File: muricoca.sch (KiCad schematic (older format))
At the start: 49 parts, among them J1 USB_B_Mini, SW1 Esc, SW10 9, SW11 0, SW12 -, SW13 =, SW14 Bksp, SW15 MXSwitch, SW16 MXSwitch, SW2 1, SW3 2, SW4 3, SW5 4, SW6 5, SW7 6, SW8 7, SW9 8, U1 ATmega32U4-AU, Y1 16Mhz

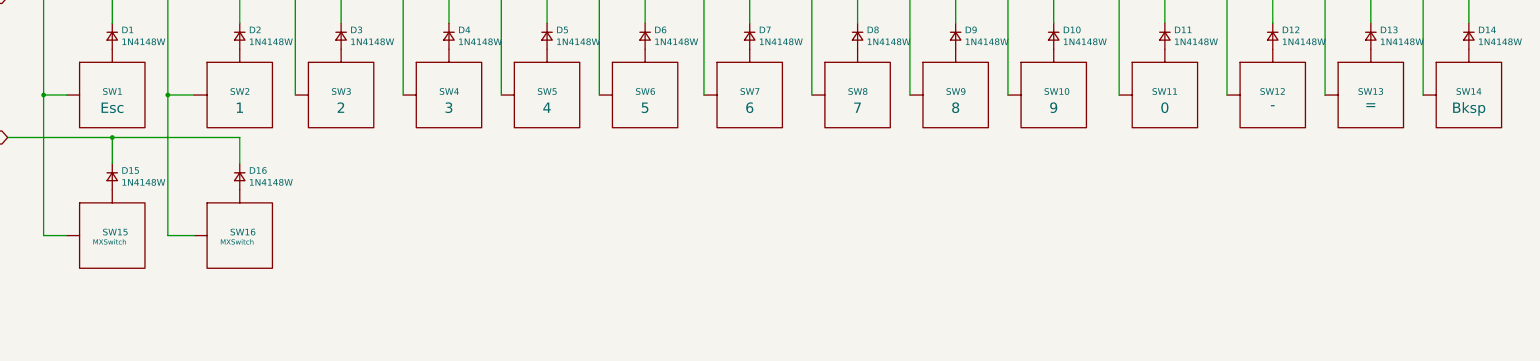
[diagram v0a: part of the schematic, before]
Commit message: feat: add matrix second row
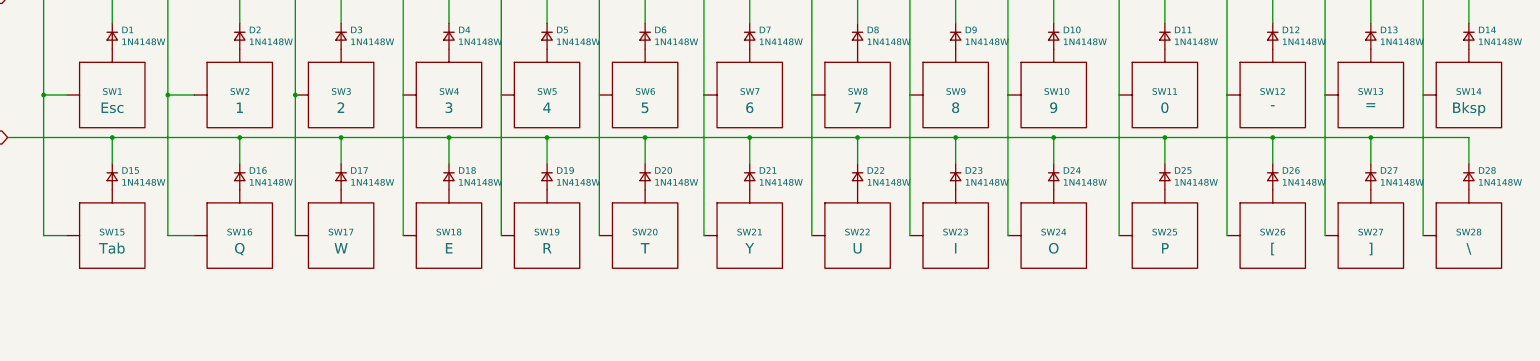
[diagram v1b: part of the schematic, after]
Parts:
- added D17, D18, D19, D20, D21, D22, D23, D24, D25, D26, D27, D28: 1N4148W, Diode_SMD:D_SOD-123, symbol Device:D_Small
- added SW17: W, acheron_MX:MX100, symbol acheronSymbols:MXSwitch
- added SW18: E, acheron_MX:MX100, symbol acheronSymbols:MXSwitch
- added SW19: R, acheron_MX:MX100, symbol acheronSymbols:MXSwitch
- added SW20: T, acheron_MX:MX100, symbol acheronSymbols:MXSwitch
- added SW21: Y, acheron_MX:MX100, symbol acheronSymbols:MXSwitch
- added SW22: U, acheron_MX:MX100, symbol acheronSymbols:MXSwitch
- added SW23: I, acheron_MX:MX100, symbol acheronSymbols:MXSwitch
- added SW24: O, acheron_MX:MX100, symbol acheronSymbols:MXSwitch
- added SW25: P, acheron_MX:MX100, symbol acheronSymbols:MXSwitch
- added SW26: [, acheron_MX:MX100, symbol acheronSymbols:MXSwitch
- added SW27: ], acheron_MX:MX100, symbol acheronSymbols:MXSwitch
- added SW28: \\, acheron_MX:MX100, symbol acheronSymbols:MXSwitch
- SW15: value MXSwitch -> Tab
- SW16: value MXSwitch -> Q
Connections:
- net COL10: now also SW24.1 (Col)
- net COL11: now also SW25.1 (Col)
- net COL12: now also SW26.1 (Col)
- net COL13: now also SW27.1 (Col)
- net COL14: now also SW28.1 (Col)
- net COL3: now also SW17.1 (Col)
- net COL4: now also SW18.1 (Col)
- net COL5: now also SW19.1 (Col)
- net COL6: now also SW20.1 (Col)
- net COL7: now also SW21.1 (Col)
- net COL8: now also SW22.1 (Col)
- net COL9: now also SW23.1 (Col)
- net ROW2: now also D17.1 (K), D18.1 (K), D19.1 (K), D20.1 (K), D21.1 (K), D22.1 (K), D23.1 (K), D24.1 (K), D25.1 (K), D26.1 (K), D27.1 (K), D28.1 (K)
- new net: D17.2 (A), SW17.2 (Row)
- new net: D18.2 (A), SW18.2 (Row)
- new net: D19.2 (A), SW19.2 (Row)
- new net: D20.2 (A), SW20.2 (Row)
- new net: D21.2 (A), SW21.2 (Row)
- new net: D22.2 (A), SW22.2 (Row)
- new net: D23.2 (A), SW23.2 (Row)
- new net: D24.2 (A), SW24.2 (Row)
- new net: D25.2 (A), SW25.2 (Row)
- new net: D26.2 (A), SW26.2 (Row)
- new net: D27.2 (A), SW27.2 (Row)
- new net: D28.2 (A), SW28.2 (Row)

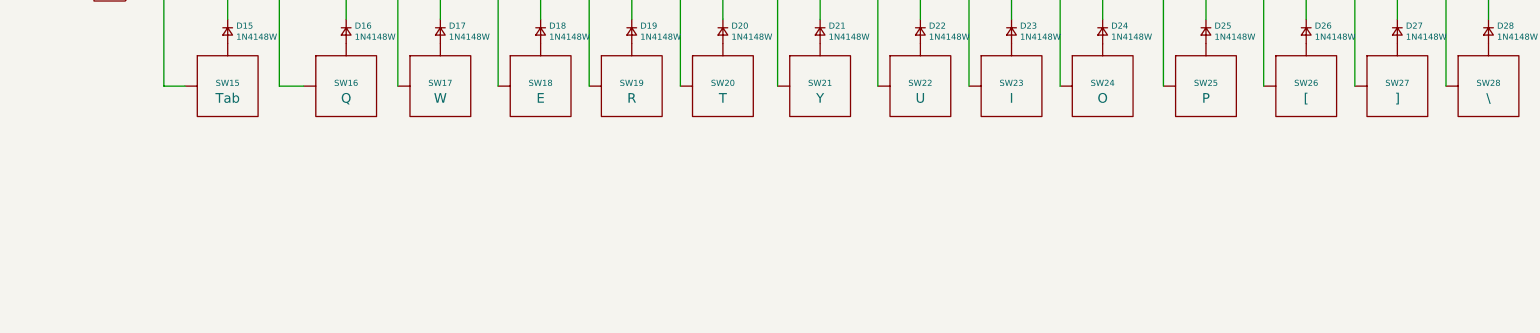
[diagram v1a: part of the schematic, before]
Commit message: feat: add matrix third row
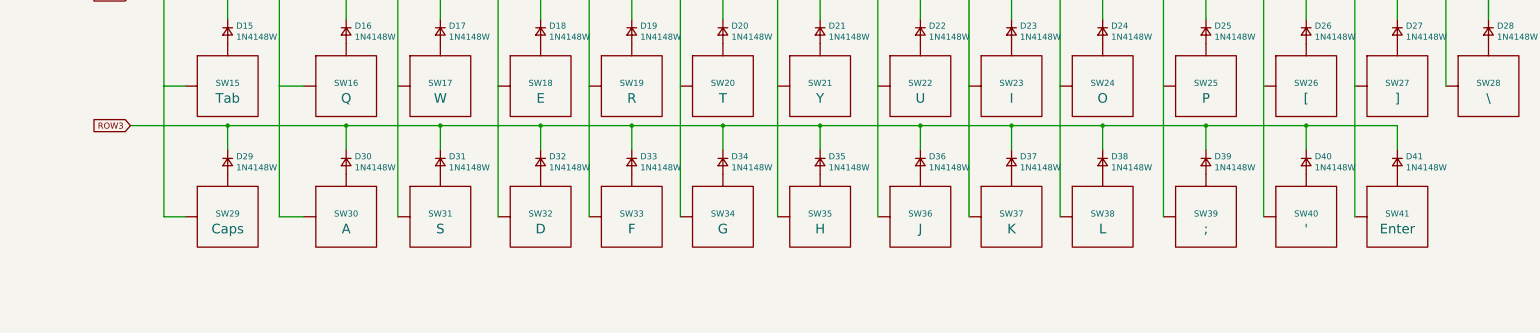
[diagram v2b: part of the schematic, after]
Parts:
- added D29, D30, D31, D32, D33, D34, D35, D36, D37, D38, D39, D40, D41: 1N4148W, Diode_SMD:D_SOD-123, symbol Device:D_Small
- added SW29: Caps, acheron_MX:MX100, symbol acheronSymbols:MXSwitch
- added SW30: A, acheron_MX:MX100, symbol acheronSymbols:MXSwitch
- added SW31: S, acheron_MX:MX100, symbol acheronSymbols:MXSwitch
- added SW32: D, acheron_MX:MX100, symbol acheronSymbols:MXSwitch
- added SW33: F, acheron_MX:MX100, symbol acheronSymbols:MXSwitch
- added SW34: G, acheron_MX:MX100, symbol acheronSymbols:MXSwitch
- added SW35: H, acheron_MX:MX100, symbol acheronSymbols:MXSwitch
- added SW36: J, acheron_MX:MX100, symbol acheronSymbols:MXSwitch
- added SW37: K, acheron_MX:MX100, symbol acheronSymbols:MXSwitch
- added SW38: L, acheron_MX:MX100, symbol acheronSymbols:MXSwitch
- added SW39: ;, acheron_MX:MX100, symbol acheronSymbols:MXSwitch
- added SW40: ', acheron_MX:MX100, symbol acheronSymbols:MXSwitch
- added SW41: Enter, acheron_MX:MX100, symbol acheronSymbols:MXSwitch
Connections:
- net COL1: now also SW29.1 (Col)
- net COL10: now also SW38.1 (Col)
- net COL11: now also SW39.1 (Col)
- net COL12: now also SW40.1 (Col)
- net COL13: now also SW41.1 (Col)
- net COL2: now also SW30.1 (Col)
- net COL3: now also SW31.1 (Col)
- net COL4: now also SW32.1 (Col)
- net COL5: now also SW33.1 (Col)
- net COL6: now also SW34.1 (Col)
- net COL7: now also SW35.1 (Col)
- net COL8: now also SW36.1 (Col)
- net COL9: now also SW37.1 (Col)
- new net: D29.2 (A), SW29.2 (Row)
- new net: D30.2 (A), SW30.2 (Row)
- new net: D31.2 (A), SW31.2 (Row)
- new net: D32.2 (A), SW32.2 (Row)
- new net: D33.2 (A), SW33.2 (Row)
- new net: D34.2 (A), SW34.2 (Row)
- new net: D35.2 (A), SW35.2 (Row)
- new net: D36.2 (A), SW36.2 (Row)
- new net: D37.2 (A), SW37.2 (Row)
- new net: D38.2 (A), SW38.2 (Row)
- new net: D39.2 (A), SW39.2 (Row)
- new net: D40.2 (A), SW40.2 (Row)
- new net: D41.2 (A), SW41.2 (Row)
- new net ROW3: D29.1 (K), D30.1 (K), D31.1 (K), D32.1 (K), D33.1 (K), D34.1 (K), D35.1 (K), D36.1 (K), D37.1 (K), D38.1 (K), D39.1 (K), D40.1 (K), D41.1 (K)

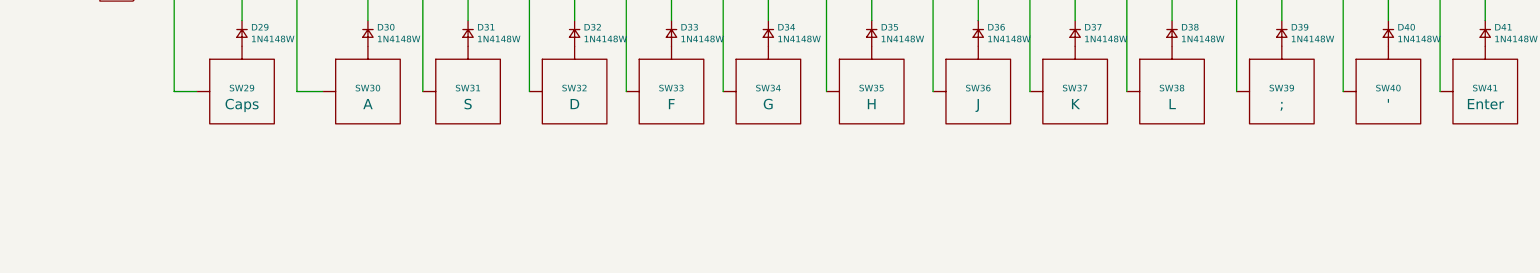
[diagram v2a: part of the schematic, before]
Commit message: feat: add matrix fourth row
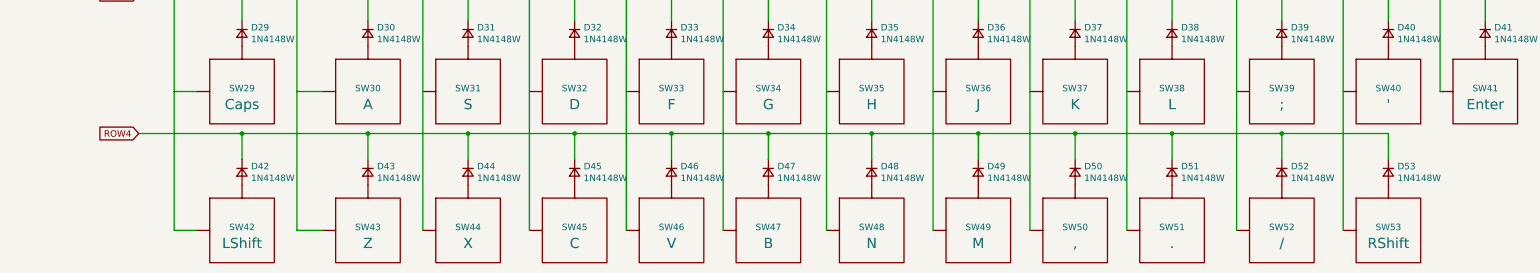
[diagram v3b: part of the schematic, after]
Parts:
- added D42, D43, D44, D45, D46, D47, D48, D49, D50, D51, D52, D53: 1N4148W, Diode_SMD:D_SOD-123, symbol Device:D_Small
- added SW42: LShift, acheron_MX:MX100, symbol acheronSymbols:MXSwitch
- added SW43: Z, acheron_MX:MX100, symbol acheronSymbols:MXSwitch
- added SW44: X, acheron_MX:MX100, symbol acheronSymbols:MXSwitch
- added SW45: C, acheron_MX:MX100, symbol acheronSymbols:MXSwitch
- added SW46: V, acheron_MX:MX100, symbol acheronSymbols:MXSwitch
- added SW47: B, acheron_MX:MX100, symbol acheronSymbols:MXSwitch
- added SW48: N, acheron_MX:MX100, symbol acheronSymbols:MXSwitch
- added SW49: M, acheron_MX:MX100, symbol acheronSymbols:MXSwitch
- added SW50: ,, acheron_MX:MX100, symbol acheronSymbols:MXSwitch
- added SW51: ., acheron_MX:MX100, symbol acheronSymbols:MXSwitch
- added SW52: /, acheron_MX:MX100, symbol acheronSymbols:MXSwitch
- added SW53: RShift, acheron_MX:MX100, symbol acheronSymbols:MXSwitch
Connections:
- net COL1: now also SW42.1 (Col)
- net COL10: now also SW51.1 (Col)
- net COL11: now also SW52.1 (Col)
- net COL12: now also SW53.1 (Col)
- net COL2: now also SW43.1 (Col)
- net COL3: now also SW44.1 (Col)
- net COL4: now also SW45.1 (Col)
- net COL5: now also SW46.1 (Col)
- net COL6: now also SW47.1 (Col)
- net COL7: now also SW48.1 (Col)
- net COL8: now also SW49.1 (Col)
- net COL9: now also SW50.1 (Col)
- new net: D42.2 (A), SW42.2 (Row)
- new net: D43.2 (A), SW43.2 (Row)
- new net: D44.2 (A), SW44.2 (Row)
- new net: D45.2 (A), SW45.2 (Row)
- new net: D46.2 (A), SW46.2 (Row)
- new net: D47.2 (A), SW47.2 (Row)
- new net: D48.2 (A), SW48.2 (Row)
- new net: D49.2 (A), SW49.2 (Row)
- new net: D50.2 (A), SW50.2 (Row)
- new net: D51.2 (A), SW51.2 (Row)
- new net: D52.2 (A), SW52.2 (Row)
- new net: D53.2 (A), SW53.2 (Row)
- new net ROW4: D42.1 (K), D43.1 (K), D44.1 (K), D45.1 (K), D46.1 (K), D47.1 (K), D48.1 (K), D49.1 (K), D50.1 (K), D51.1 (K), D52.1 (K), D53.1 (K)

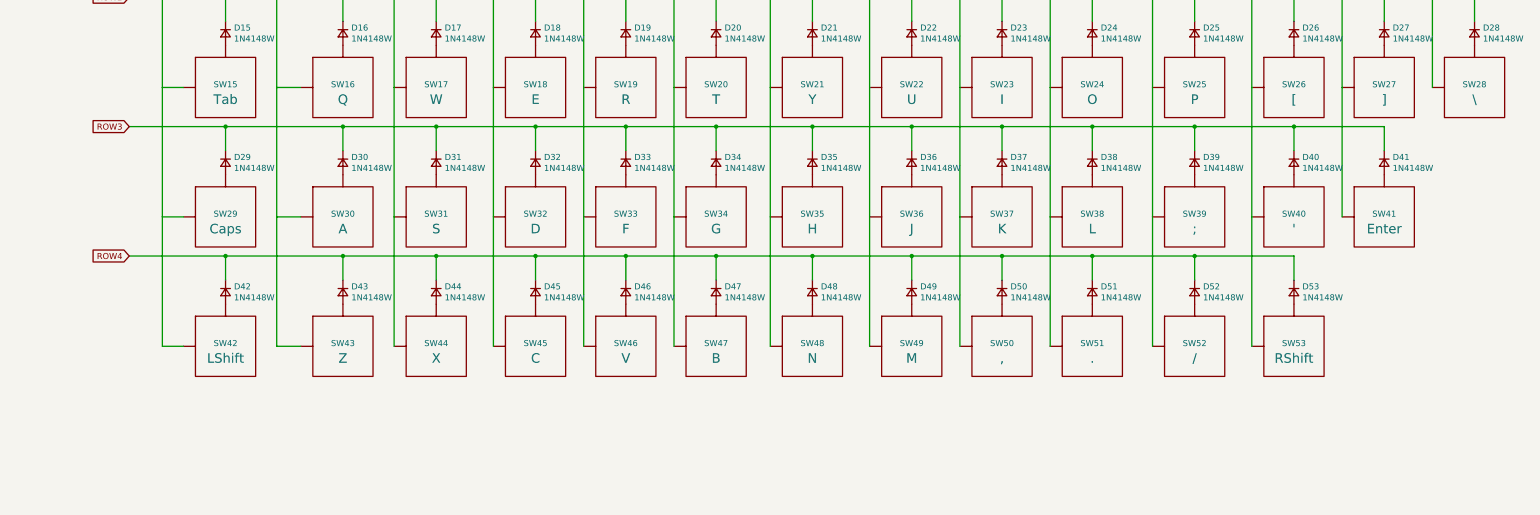
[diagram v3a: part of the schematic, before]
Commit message: feat: add matrix fifth row
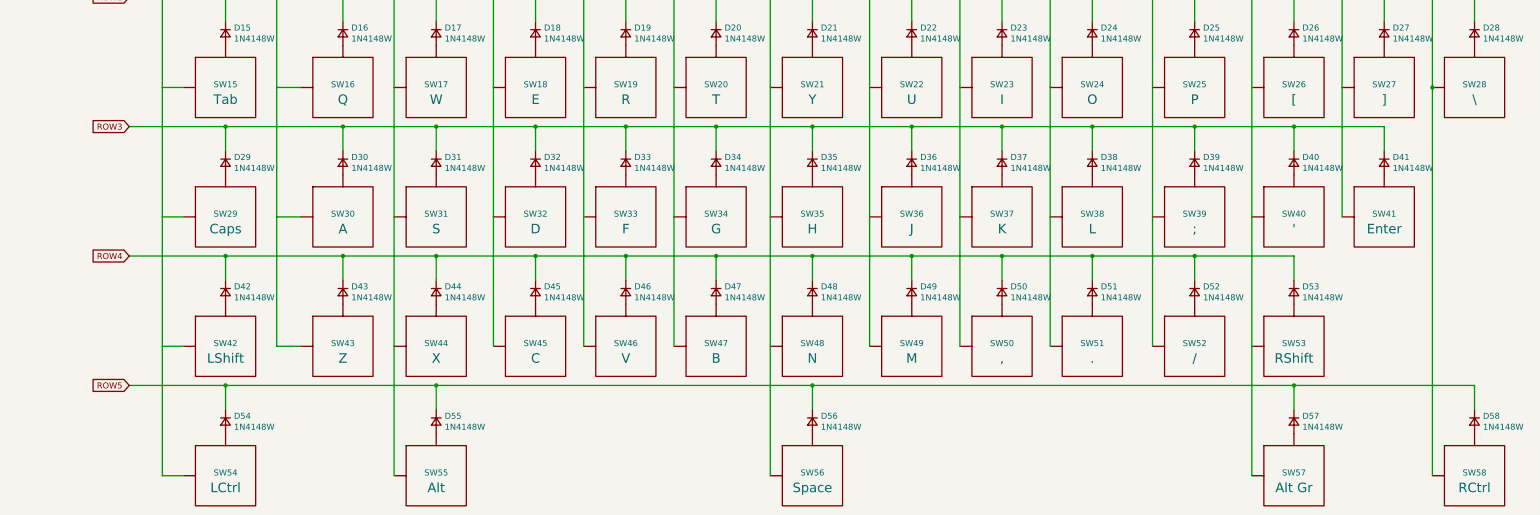
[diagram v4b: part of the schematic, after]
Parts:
- added D54, D55, D56, D57, D58: 1N4148W, Diode_SMD:D_SOD-123, symbol Device:D_Small
- added SW54: LCtrl, acheron_MX:MX100, symbol acheronSymbols:MXSwitch
- added SW55: Alt, acheron_MX:MX100, symbol acheronSymbols:MXSwitch
- added SW56: Space, acheron_MX:MX100, symbol acheronSymbols:MXSwitch
- added SW57: Alt Gr, acheron_MX:MX100, symbol acheronSymbols:MXSwitch
- added SW58: RCtrl, acheron_MX:MX100, symbol acheronSymbols:MXSwitch
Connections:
- net COL1: now also SW54.1 (Col)
- net COL12: now also SW57.1 (Col)
- net COL14: now also SW58.1 (Col)
- net COL3: now also SW55.1 (Col)
- net COL7: now also SW56.1 (Col)
- new net: D54.2 (A), SW54.2 (Row)
- new net: D55.2 (A), SW55.2 (Row)
- new net: D56.2 (A), SW56.2 (Row)
- new net: D57.2 (A), SW57.2 (Row)
- new net: D58.2 (A), SW58.2 (Row)
- new net ROW5: D54.1 (K), D55.1 (K), D56.1 (K), D57.1 (K), D58.1 (K)
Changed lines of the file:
@@
 	1    0    0    -1
 $EndComp
+$Comp
+L Device:D_Small D54
+U 1 1 5F1622F0
+P 8575 6800
+F 0 "D54" V 8529 6870 50  0000 L CNN
+F 1 "1N4148W" V 8620 6870 50  0000 L CNN
+F 2 "Diode_SMD:D_SOD-123" V 8575 6800 50  0001 C CNN
+F 3 "~" V 8575 6800 50  0001 C CNN
+	1    8575 6800
+	0    1    1    0
+$EndComp
+Wire Wire Line
+	8575 6700 8575 6500
+Connection ~ 8575 6500
+Wire Wire Line
+	8575 6500 7775 6500
+Wire Wire Line
+	8225 7250 8050 7250
+Wire Wire Line
+	8050 7250 8050 6175
+Text GLabel 7775 6500 0    50   Input ~ 0
+ROW5
+Wire Wire Line
+	9975 6175 9975 7250
+$Comp
+L Device:D_Small D55
+U 1 1 5F162313
+P 10325 6800
+F 0 "D55" V 10279 6870 50  0000 L CNN
+F 1 "1N4148W" V 10370 6870 50  0000 L CNN
+F 2 "Diode_SMD:D_SOD-123" V 10325 6800 50  0001 C CNN
+F 3 "~" V 10325 6800 50  0001 C CNN
+	1    10325 6800
+	0    1    1    0
+$EndComp
+Wire Wire Line
+	13100 6175 13100 7250
+$Comp
+L acheronSymbols:MXSwitch SW56
+U 1 1 5F16233B
+P 13450 7250
+F 0 "SW56" H 13450 7275 50  0000 C CNN
+F 1 "Space" H 13450 7150 79  0000 C CNN
+F 2 "acheron_MX:MX100" H 13450 7250 50  0001 C CNN
+F 3 "" H 13450 7250 50  0001 C CNN
+	1    13450 7250
+	1    0    0    -1
+$EndComp
+$Comp
+L Device:D_Small D56
+U 1 1 5F162341
+P 13450 6800
+F 0 "D56" V 13404 6870 50  0000 L CNN
+F 1 "1N4148W" V 13495 6870 50  0000 L CNN
+F 2 "Diode_SMD:D_SOD-123" V 13450 6800 50  0001 C CNN
+F 3 "~" V 13450 6800 50  0001 C CNN
+	1    13450 6800
+	0    1    1    0
+$EndComp
+Wire Wire Line
+	17100 6175 17100 7250
+$Comp
+L acheronSymbols:MXSwitch SW57
+U 1 1 5F16237C
+P 17450 7250
+F 0 "SW57" H 17450 7275 50  0000 C CNN
+F 1 "Alt Gr" H 17450 7150 79  0000 C CNN
+F 2 "acheron_MX:MX100" H 17450 7250 50  0001 C CNN
+F 3 "" H 17450 7250 50  0001 C CNN
+	1    17450 7250
+	1    0    0    -1
+$EndComp
+$Comp
+L Device:D_Small D57
+U 1 1 5F162382
+P 17450 6800
+F 0 "D57" V 17404 6870 50  0000 L CNN
+F 1 "1N4148W" V 17495 6870 50  0000 L CNN
+F 2 "Diode_SMD:D_SOD-123" V 17450 6800 50  0001 C CNN
+F 3 "~" V 17450 6800 50  0001 C CNN
+	1    17450 6800
+	0    1    1    0
+$EndComp
+Wire Wire Line
+	10325 6700 10325 6500
+Connection ~ 10325 6500
+Wire Wire Line
+	13450 6700 13450 6500
+Connection ~ 13450 6500
+Wire Wire Line
+	17450 6700 17450 6500
+$Comp
+L acheronSymbols:MXSwitch SW54
+U 1 1 5F1623AC
+P 8575 7250
+F 0 "SW54" H 8575 7275 50  0000 C CNN
+F 1 "LCtrl" H 8575 7150 79  0000 C CNN
+F 2 "acheron_MX:MX100" H 8575 7250 50  0001 C CNN
+F 3 "" H 8575 7250 50  0001 C CNN
+	1    8575 7250
+	1    0    0    -1
+$EndComp
+Wire Wire Line
+	8575 6500 10325 6500
+$Comp
+L acheronSymbols:MXSwitch SW55
+U 1 1 5F16230D
+P 10325 7250
+F 0 "SW55" H 10325 7275 50  0000 C CNN
+F 1 "Alt" H 10325 7150 79  0000 C CNN
+F 2 "acheron_MX:MX100" H 10325 7250 50  0001 C CNN
+F 3 "" H 10325 7250 50  0001 C CNN
+	1    10325 7250
+	1    0    0    -1
+$EndComp
+Wire Wire Line
+	10325 6500 13450 6500
+Wire Wire Line
+	13450 6500 17450 6500
+$Comp
+L acheronSymbols:MXSwitch SW58
+U 1 1 5F1D2F49
+P 18950 7250
+F 0 "SW58" H 18950 7275 50  0000 C CNN
+F 1 "RCtrl" H 18950 7150 79  0000 C CNN
+F 2 "acheron_MX:MX100" H 18950 7250 50  0001 C CNN
+F 3 "" H 18950 7250 50  0001 C CNN
+	1    18950 7250
+	1    0    0    -1
+$EndComp
+$Comp
+L Device:D_Small D58
+U 1 1 5F1D2F4F
+P 18950 6800
+F 0 "D58" V 18904 6870 50  0000 L CNN
+F 1 "1N4148W" V 18995 6870 50  0000 L CNN
+F 2 "Diode_SMD:D_SOD-123" V 18950 6800 50  0001 C CNN
+F 3 "~" V 18950 6800 50  0001 C CNN
+	1    18950 6800
+	0    1    1    0
+$EndComp
+Wire Wire Line
+	18600 4025 18600 7250
+Connection ~ 18600 4025
+Wire Wire Line
+	17450 6500 18950 6500
+Wire Wire Line
+	18950 6500 18950 6700
+Connection ~ 17450 6500
 $EndSCHEMATC
